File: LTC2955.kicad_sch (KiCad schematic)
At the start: 21 parts, among them SW4 SW_Push, U4 LTC2955CTS8-2_TRPBF

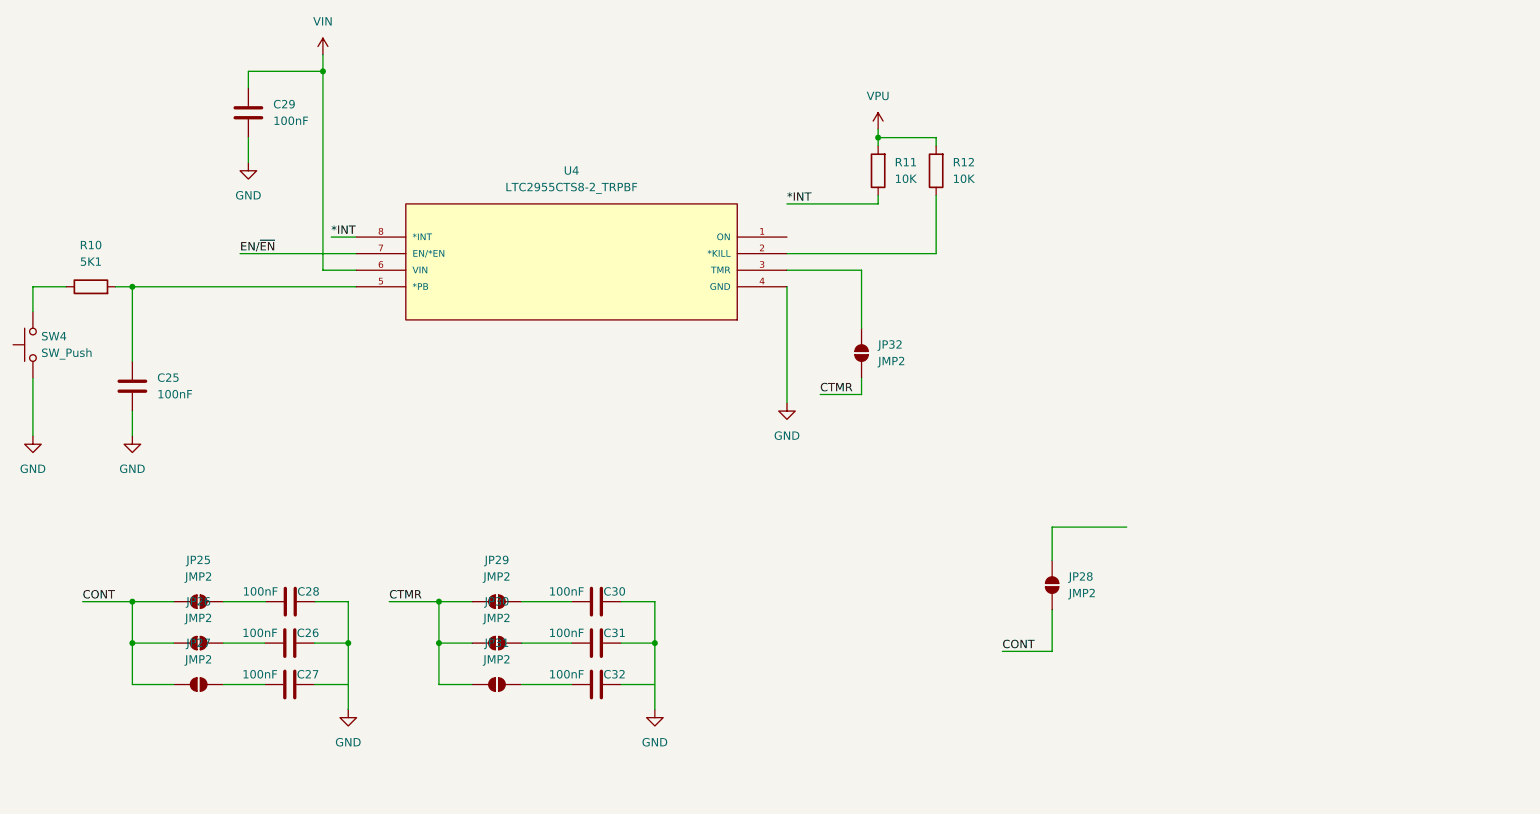
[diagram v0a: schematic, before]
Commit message: Added B.O.M, TODO: do PCB track layout
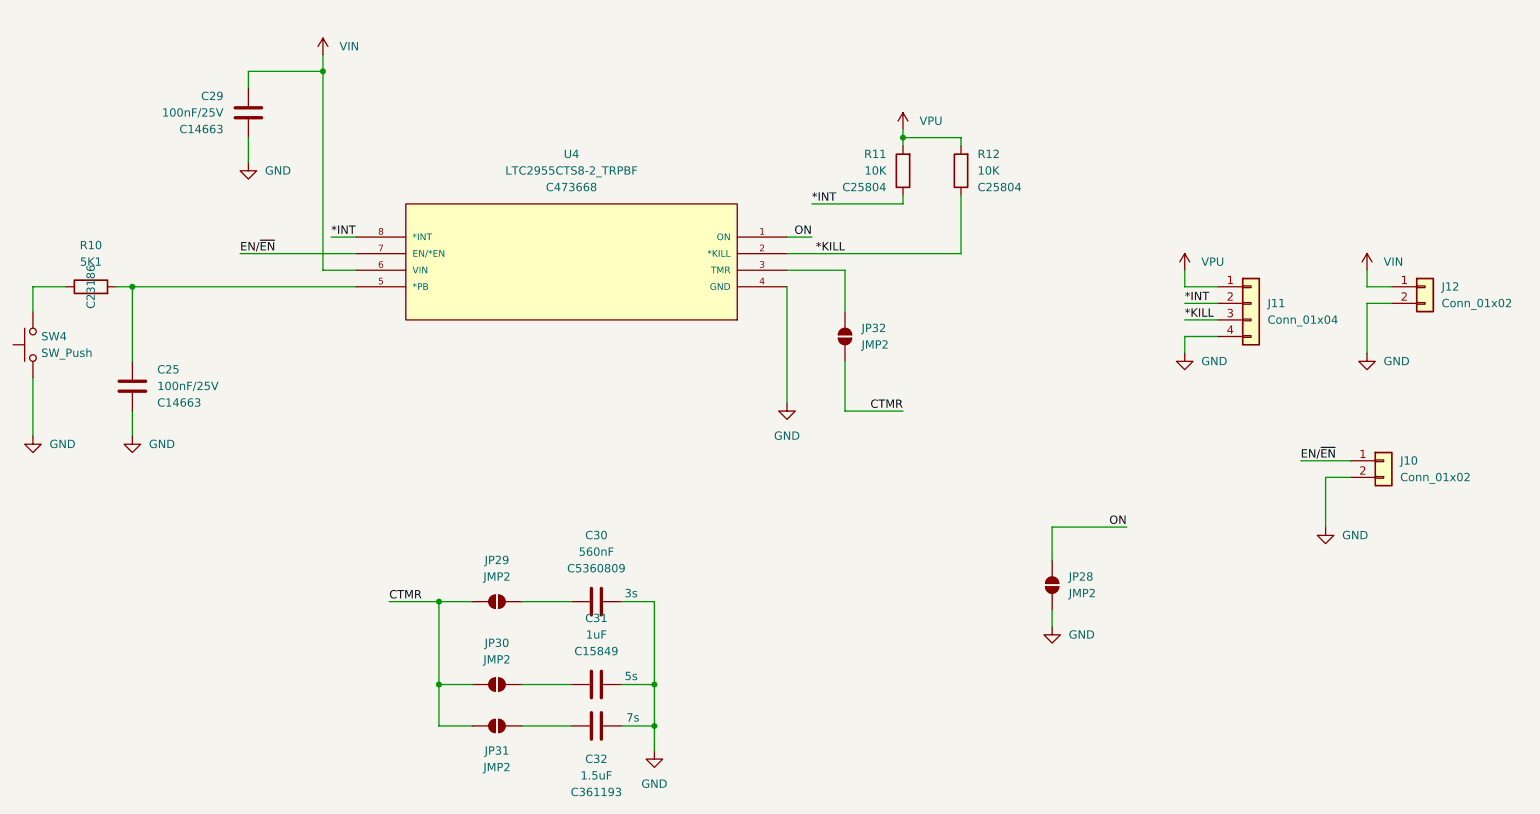
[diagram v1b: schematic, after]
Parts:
- removed C26, C27, C28: 100nF, Capacitor_SMD:C_0603_1608Metric, symbol Device:C
- removed JP25, JP26, JP27: JMP2, Jumper:SolderJumper-2_P1.3mm_Open_RoundedPad1.0x1.5mm, symbol Jumper:SolderJumper_2_Open
- added J10, J12: Conn_01x02, Connector_PinHeader_2.54mm:PinHeader_1x02_P2.54mm_Vertical, symbol Connector_Generic:Conn_01x02
- added J11: Conn_01x04, Connector_PinHeader_2.54mm:PinHeader_1x04_P2.54mm_Vertical, symbol Connector_Generic:Conn_01x04
- C25, C29: value 100nF -> 100nF/25V; JLCPCB Part # (none) -> C14663
- C30: value 100nF -> 560nF; JLCPCB Part # (none) -> C5360809
- C31: value 100nF -> 1uF; JLCPCB Part # (none) -> C15849
- C32: value 100nF -> 1.5uF; JLCPCB Part # (none) -> C361193
- R10: JLCPCB Part # (none) -> C23186
- R11, R12: JLCPCB Part # (none) -> C25804
- U4: JLCPCB Part # (none) -> C473668
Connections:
- net CONT is gone; now on net GND: JP28.1 (A)
- net *INT: now also J11.2 (Pin_2)
- net EN/~{EN}: now also J10.1 (Pin_1)
- net GND: now also C32.2, J10.2 (Pin_2), J11.4 (Pin_4), J12.2 (Pin_2)
- net VIN: now also J12.1 (Pin_1)
- net VPU: now also J11.1 (Pin_1)
- net ON: now reaches U4.1 (ON)
- net ON: now also JP28.2 (B)
- net *KILL: now reaches R12.1, U4.2 (*KILL)
- net *KILL: now also J11.3 (Pin_3)
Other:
- note added: "3s"
- note added: "5s"
- note added: "7s"
- moved on the sheet: C31, C32, JP30, JP31, JP32, R11, R12
